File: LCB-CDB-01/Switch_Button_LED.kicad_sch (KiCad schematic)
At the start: 67 parts, among them J1 01x02, J10 01x02, J11 01x02, J12 01x02, J13 01x02, J14 01x02, J15 01x02, J16 01x02, J17 01x02, J18 01x02, J19 01x02, J2 01x02, J20 01x02, J21 01x02, J22 01x02, J23 01x02, J24 01x02, J25 01x02, J26 01x02, J27 01x02, J28 01x02, J29 01x02, J3 01x02, J30 01x02, J4 01x02, J5 01x02, J6 01x02, J7 01x02, J8 01x02, J9 01x02

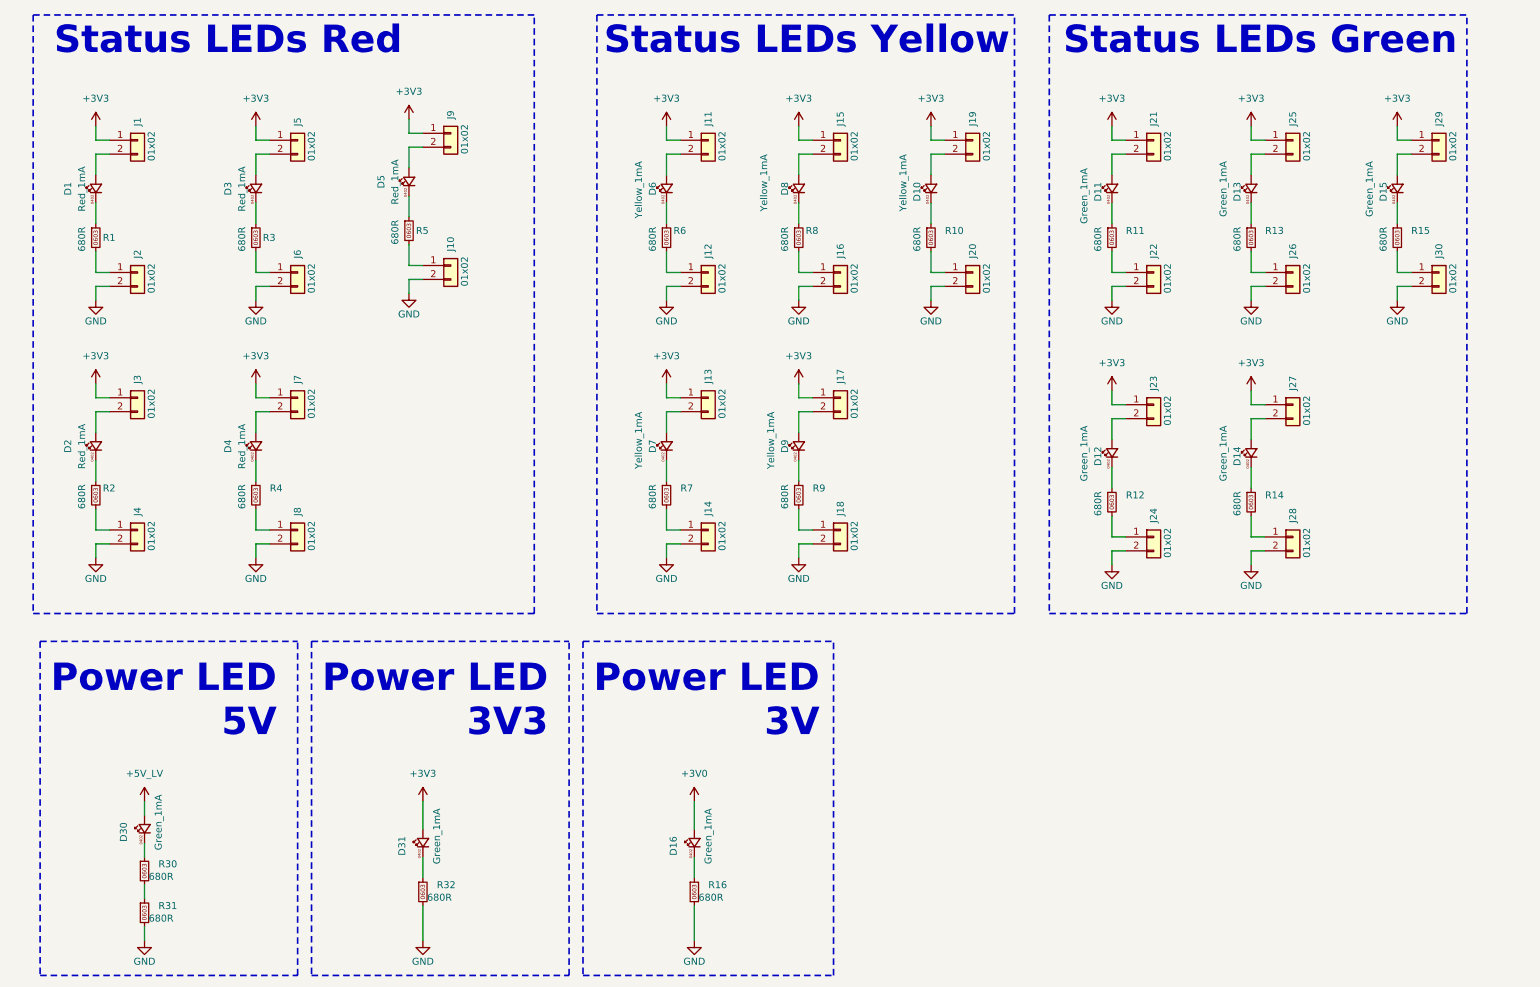
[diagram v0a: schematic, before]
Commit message: update symbols and footprints to latest library
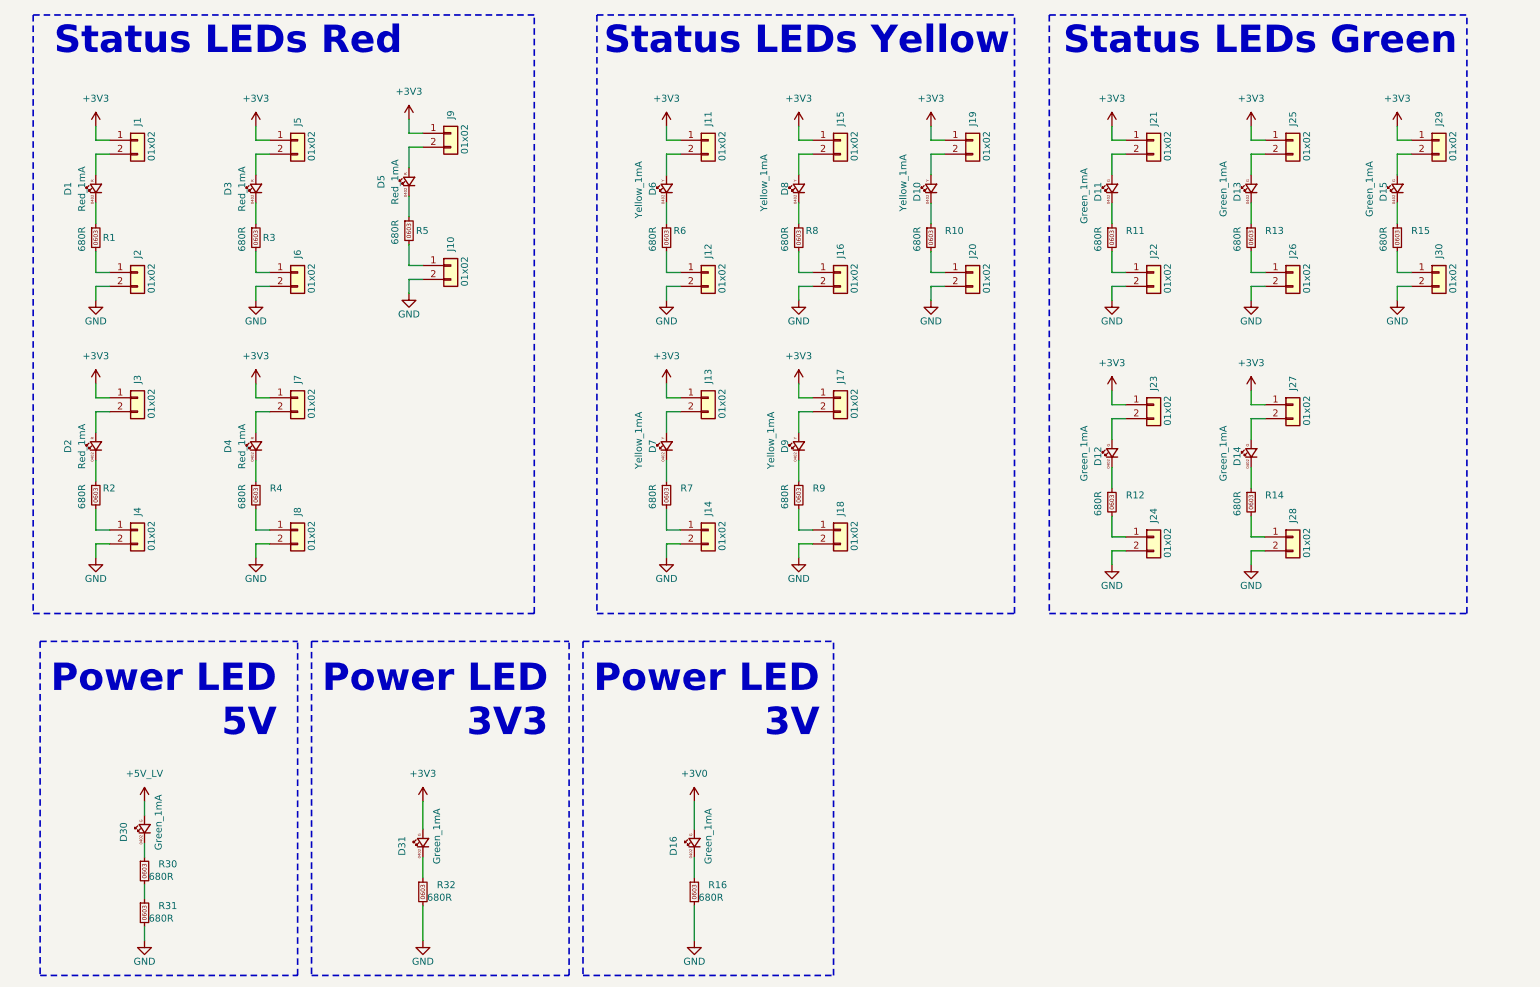
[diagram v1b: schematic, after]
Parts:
- D1, D2, D3, D4, D5: footprint LEA_FootprintLibrary:LED_0402 -> LEA_FootprintLibrary:LED_0402_R
- D10, D6, D7, D8, D9: footprint LEA_FootprintLibrary:LED_0402 -> LEA_FootprintLibrary:LED_0402_Y
- D11, D12, D13, D14, D15, D16, D30, D31: footprint LEA_FootprintLibrary:LED_0402 -> LEA_FootprintLibrary:LED_0402_G
